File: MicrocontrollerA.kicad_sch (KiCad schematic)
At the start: 28 parts, among them J1 SWD Connector, SW1 SW_Push, SW2 SW_SPDT, SW3 SW_SPDT, U1 STM32F446RCTx, Y1 25 MHz

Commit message: Change magnetometer interface from I2C to SPI
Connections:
- net SPI1_CS2: now reaches U1.38 (PC7)
- no-connect marks 22 -> 21

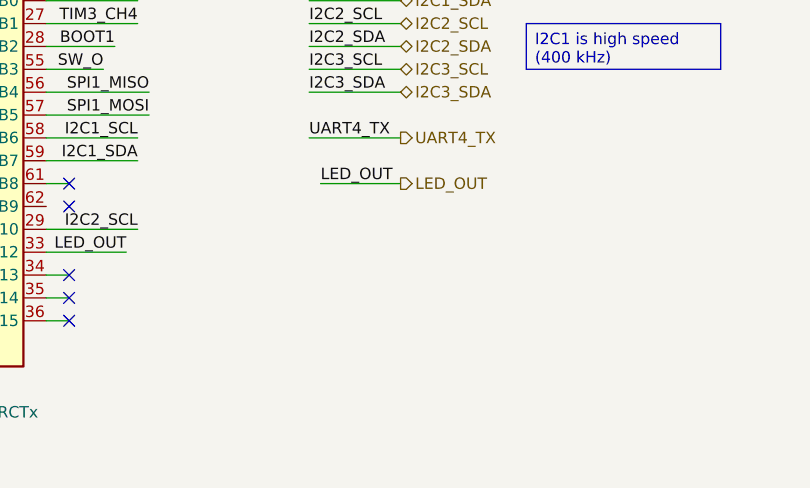
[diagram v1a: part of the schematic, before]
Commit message: Add indicator LED for MCU A
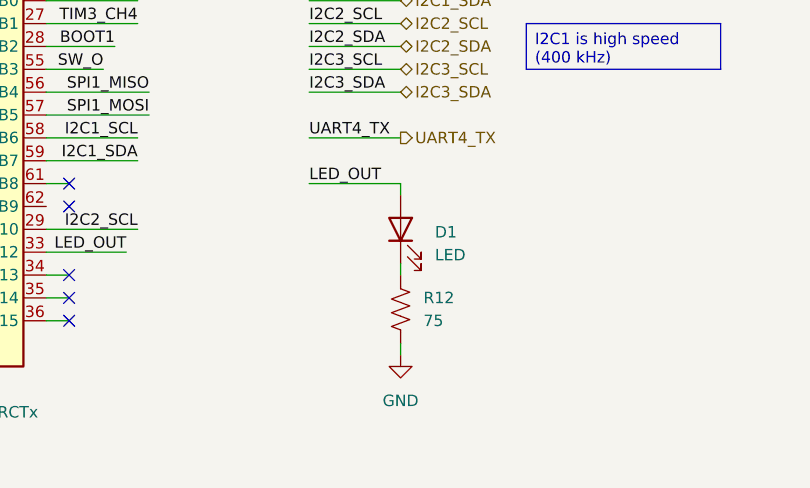
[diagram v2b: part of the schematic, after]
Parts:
- added D1: LED, symbol Device:LED
- added R12: 75, symbol Device:R_US
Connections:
- net GND: now also R12.2
- net LED_OUT: now also D1.2 (A)
- new net: D1.1 (K), R12.1

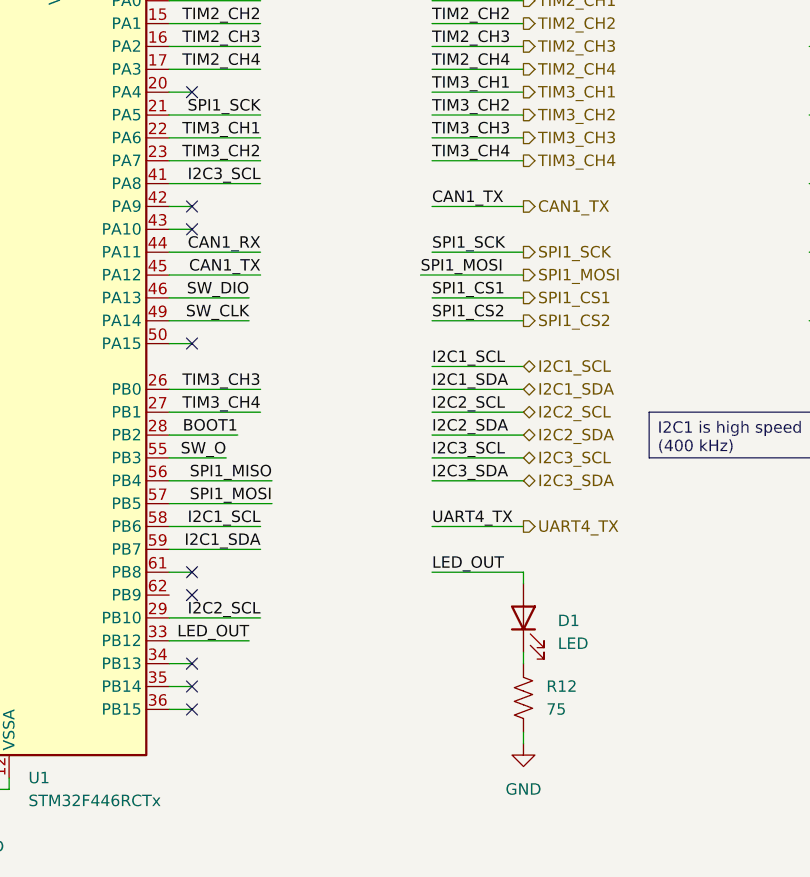
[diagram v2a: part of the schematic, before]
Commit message: Add thruster pin outputs
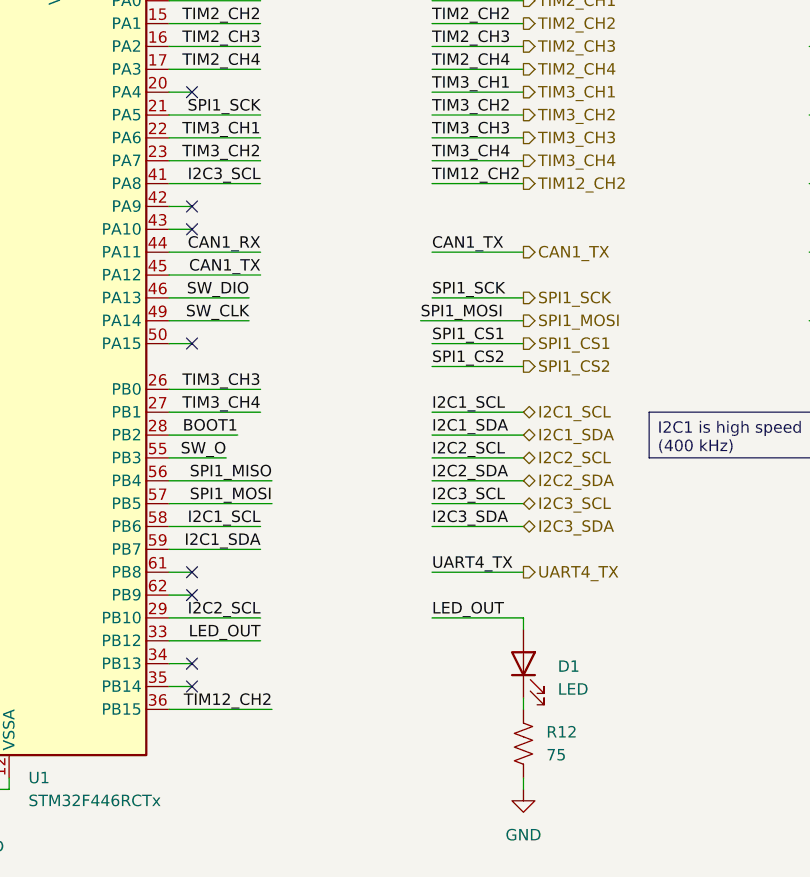
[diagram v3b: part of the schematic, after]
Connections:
- net TIM12_CH2: now reaches U1.36 (PB15)
- no-connect marks 21 -> 20
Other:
- moved on the sheet: D1, R12

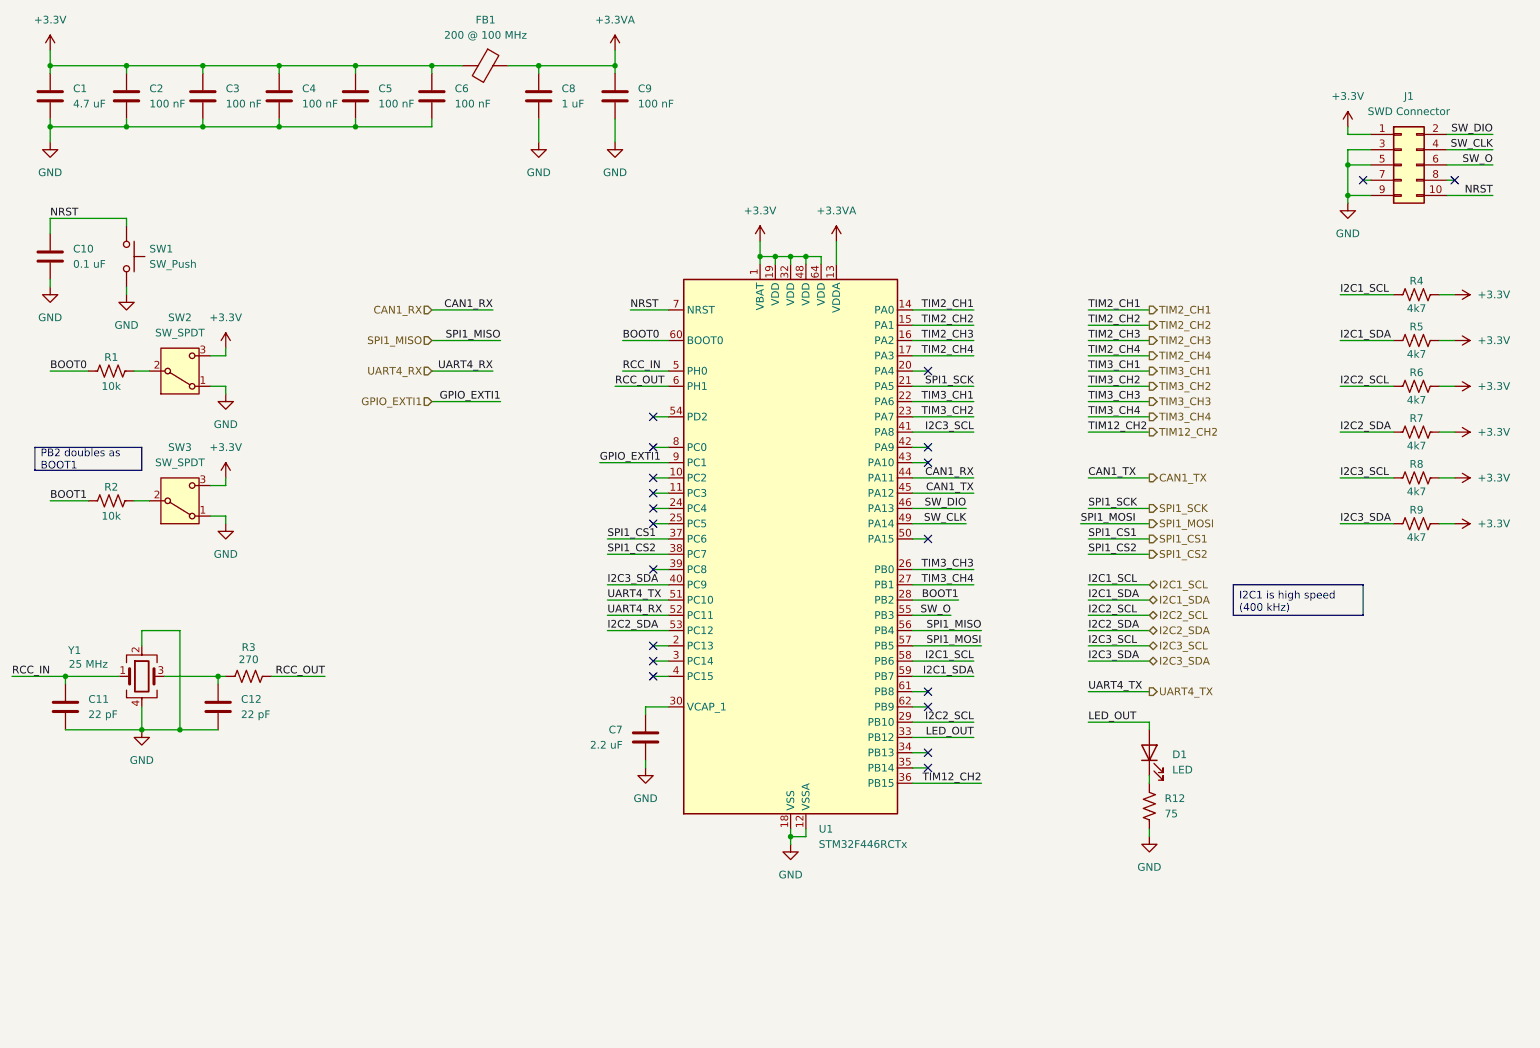
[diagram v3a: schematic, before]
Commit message: Remove unused I2C pins and add USB
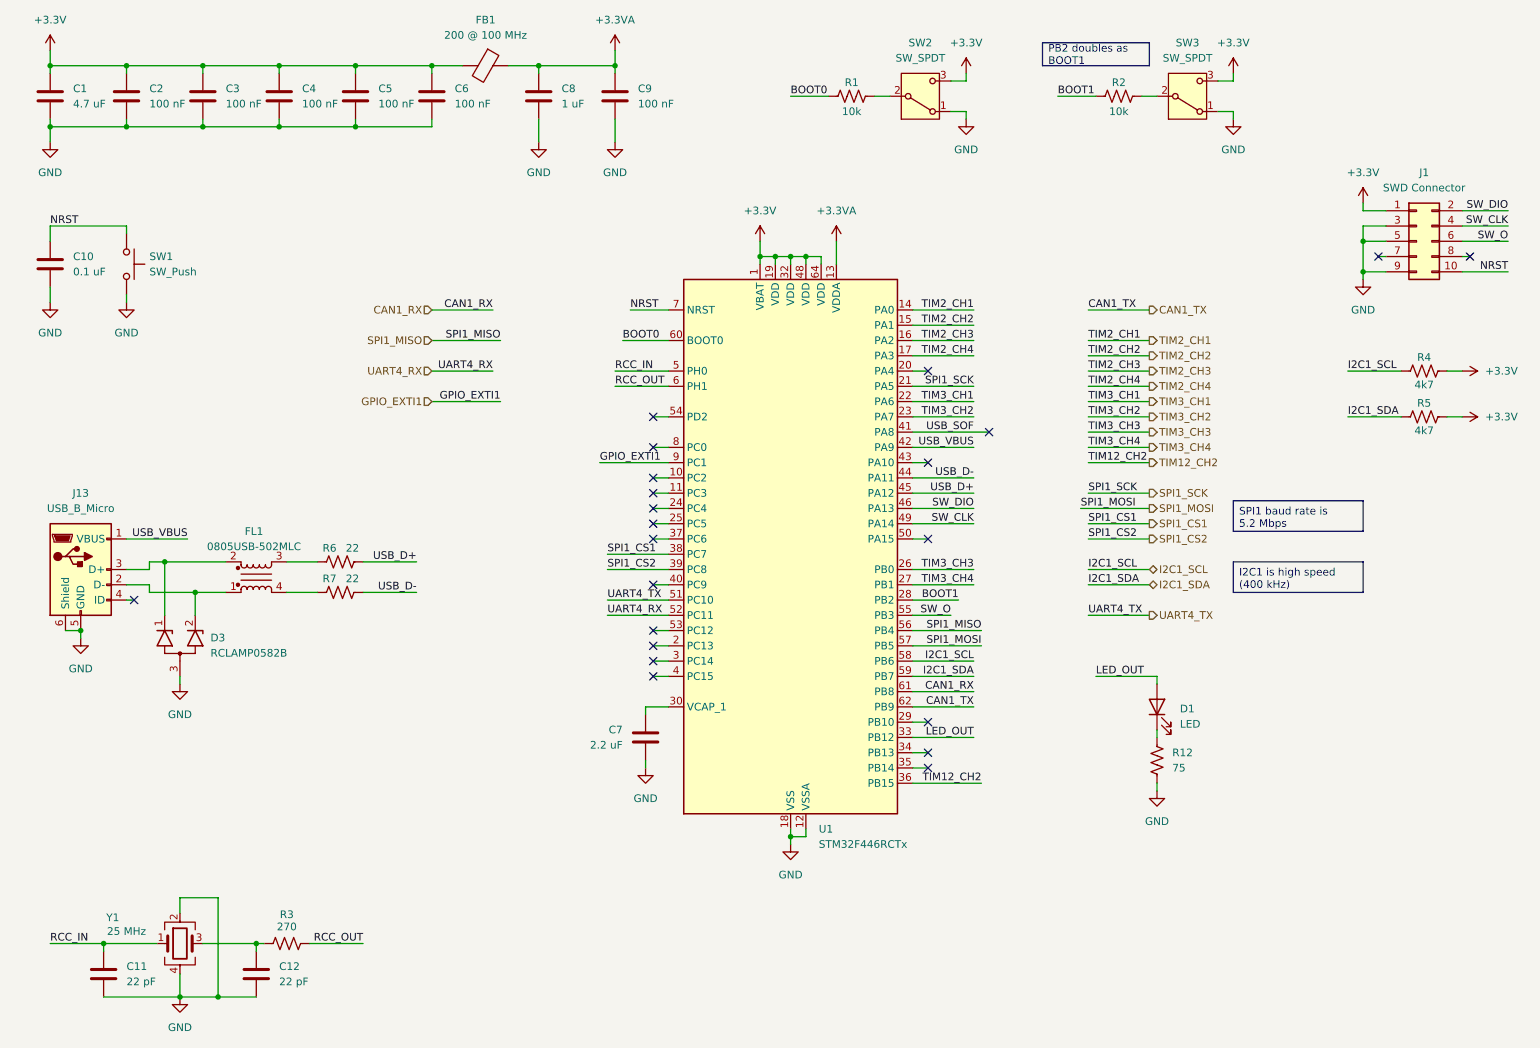
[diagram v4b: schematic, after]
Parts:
- removed R8, R9: 4k7, symbol Device:R_US
- added D3: RCLAMP0582B, Package_TO_SOT_SMD:SOT-416, symbol Power_Protection:RCLAMP0582B
- added FL1: 0805USB-502MLC, Inductor_SMD:L_CommonModeChoke_Coilcraft_0805USB, symbol Device:Filter_EMI_LL_1423
- added J13: USB_B_Micro, symbol Connector:USB_B_Micro
- R6, R7: value 4k7 -> 22
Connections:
- net +3.3V: no longer R6.1, R7.1
- net CAN1_RX: now also U1.61 (PB8); no longer U1.44 (PA11)
- net CAN1_TX: now also U1.62 (PB9); no longer U1.45 (PA12)
- net GND: now also D3.3 (A), J13.5 (GND), J13.6 (Shield)
- net SPI1_CS1: now also U1.38 (PC7); no longer U1.37 (PC6)
- net SPI1_CS2: now also U1.39 (PC8); no longer U1.38 (PC7)
- net USB_VBUS: now reaches U1.42 (PA9)
- net USB_VBUS: now also J13.1 (VBUS)
- net I2C2_SCL: no longer names the net of U1.29 (PB10)
- net I2C2_SCL: no longer R6.2
- net I2C2_SDA: no longer names the net of U1.53 (PC12)
- net I2C2_SDA: no longer R7.2
- net I2C3_SCL renamed USB_SOF
- net I2C3_SDA: no longer names the net of U1.40 (PC9)
- new net: D3.1 (K1), FL1.2, J13.3 (D+)
- new net: D3.2 (K2), FL1.1, J13.2 (D-)
- new net: FL1.4, R7.2
- new net: FL1.3, R6.2
- new net USB_D+: R6.1, U1.45 (PA12)
- new net USB_D-: R7.1, U1.44 (PA11)
- no-connect marks 20 -> 22
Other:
- moved on the sheet: C10, C11, C12, D1, J1, R1, R12, R2, R3, R4, R5, SW1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

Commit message: Add footprints to symbols
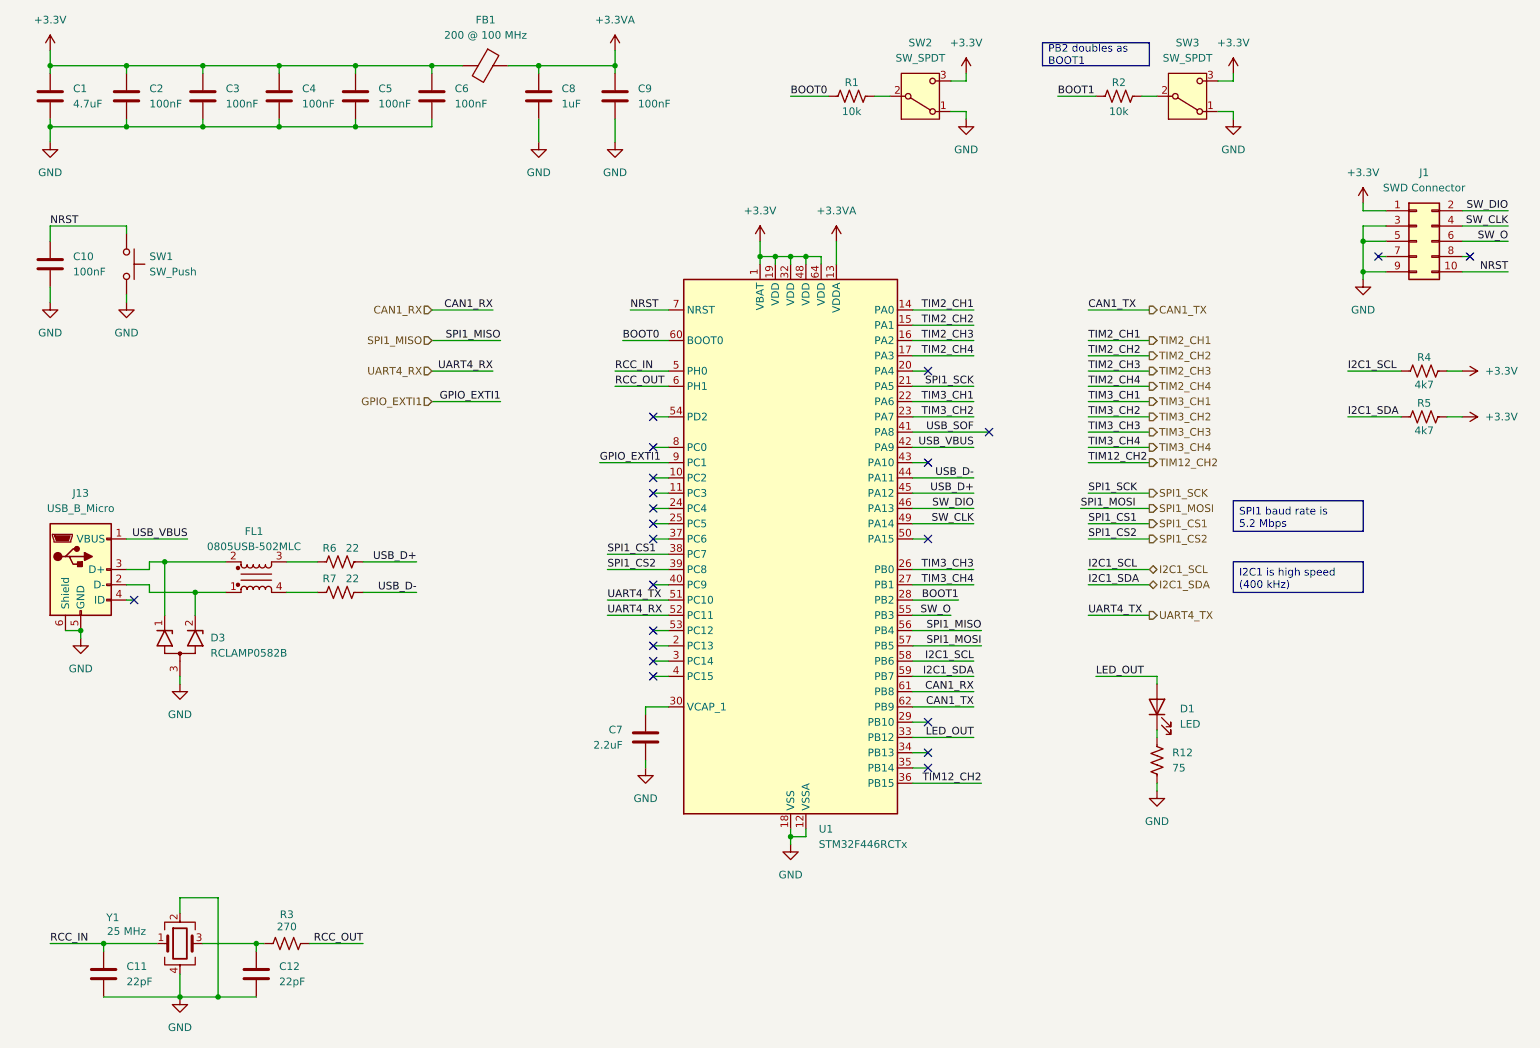
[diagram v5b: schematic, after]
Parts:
- C1: value 4.7 uF -> 4.7uF; footprint (none) -> Capacitor_SMD:C_0603_1608Metric; Listing (none) -> https://www.digikey.com/en/products/detail/samsung-electro-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
- C10: value 0.1 uF -> 100nF; footprint (none) -> Capacitor_SMD:C_0402_1005Metric; Listing (none) -> https://www.digikey.com/en/products/detail/samsung-electro-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
- C11, C12: value 22 pF -> 22pF; footprint (none) -> Capacitor_SMD:C_0402_1005Metric; Listing (none) -> https://www.digikey.com/en/products/detail/kyocera-avx/600L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
- C2, C3, C4, C5, C6, C9: value 100 nF -> 100nF; footprint (none) -> Capacitor_SMD:C_0402_1005Metric; Listing (none) -> https://www.digikey.com/en/products/detail/samsung-electro-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
- C7: value 2.2 uF -> 2.2uF; footprint (none) -> Capacitor_SMD:C_0603_1608Metric; Listing (none) -> https://www.digikey.com/en/products/detail/samsung-electro-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
- C8: value 1 uF -> 1uF; footprint (none) -> Capacitor_SMD:C_0603_1608Metric; Listing (none) -> https://www.digikey.com/en/products/detail/samsung-electro-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
- D1: footprint (none) -> LED_SMD:LED_0603_1608Metric; Listing (none) -> https://www.digikey.com/en/products/detail/liteon/LTST-C190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
- D3: Listing (none) -> https://www.digikey.com/en/products/detail/semtech-corporat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
- FB1: footprint (none) -> Inductor_SMD:L_0805_2012Metric; Listing (none) -> https://www.digikey.com/en/products/detail/laird-signal-int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
- FL1: Listing (none) -> https://www.mouser.com/ProductDetail/Coilcraft/0805USB-502M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
- J1: footprint (none) -> Connector_IDC:IDC-Header_2x05_P2.54mm_Vertical; Listing (none) -> https://www.digikey.com/en/products/detail/3m/N2510-6002-RB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
- J13: footprint (none) -> Connector_USB:USB_Micro-B_Molex_47346-0001; Listing (none) -> https://www.digikey.com/en/products/detail/molex/0473460001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
- R1, R2, R6, R7: footprint (none) -> Resistor_SMD:R_0402_1005Metric; Listing (none) -> https://www.digikey.com/en/products/detail/yageo/RC0402FR-0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
- R12, R4, R5: footprint (none) -> Resistor_SMD:R_0402_1005Metric; Listing (none) -> https://www.digikey.com/en/products/detail/yageo/RC0402JR-0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
- R3: footprint (none) -> Resistor_SMD:R_0402_1005Metric; Listing (none) -> https://www.digikey.com/en/products/detail/stackpole-electr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
- SW1: footprint (none) -> Button_Switch_SMD:SW_Push_1P1T_NO_E-Switch_TL3301NxxxxxG; Listing (none) -> https://www.digikey.com/en/products/detail/e-switch/TL3301N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
- SW2, SW3: footprint (none) -> Button_Switch_SMD:Nidec_Copal_CAS-120A; Listing (none) -> https://www.digikey.com/en/products/detail/nidec-components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
- U1: Listing (none) -> https://www.digikey.com/en/products/detail/stmicroelectroni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
- Y1: Digikey https://www.digikey.com/en/products/detail/abracon-llc/ABM8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 -> (none); Listing (none) -> https://www.digikey.com/en/products/detail/abracon-llc/ABM8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
